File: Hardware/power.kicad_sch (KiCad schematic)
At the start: 18 parts, among them J3 JST_2mm_LiPo, U1 AP2112K-3.3, U2 MAX17048, U3 MCP73831

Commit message: Change to dedicated header format.
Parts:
- added D2: BAT60A, SparkFun-Semiconductor-Standard:SOD-323, symbol SparkFun-DiscreteSemi:D_Schottky_3A_10V_0.28V
- added J2: 1x10, SparkFun-Connector:1x10_Locking, symbol SparkFun-Connector:GNSS_Shield_10
- added J4: 1x09, SparkFun-Connector:1x09_Locking, symbol SparkFun-Connector:GNSS_Shield_9
- R13: value 10k -> 100k; symbol SparkFun-Resistor:10k_0603 -> SparkFun-Resistor:100k_0603; PROD_ID RES-00824 -> RES-07828
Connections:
- net 3V3_EN: now also J2.2 (Pin_2)
- net 5V: now also D2.C, J4.2 (Pin_8)
- net GND: now also J2.10 (Pin_10), J4.1 (Pin_9)
- net SCL: now also J2.7 (Pin_7)
- net SDA: now also J2.8 (Pin_8)
- net VBATT: now also D2.A
- new net Main-RX: J4.4 (Pin_6)
- new net Main-TX: J4.5 (Pin_5)
- new net SD_CD: J2.6 (Pin_6)
- new net SHLD_PICO: J4.7 (Pin_3)
- new net SHLD_POCI: J4.8 (Pin_2)
- new net SHLD_SCK: J4.9 (Pin_1)
- new net SHLD_~{CS}: J4.6 (Pin_4)
- no-connect marks 1 -> 6
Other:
- note added: "If 5V is present, LiPo charging commences. If 5V is absent, battery provides VBATT to mainboard. 3.3V is not provided to mainboard. 5V/VBATT powers local 3.3V_P."
- note added: "Shield Connectors"

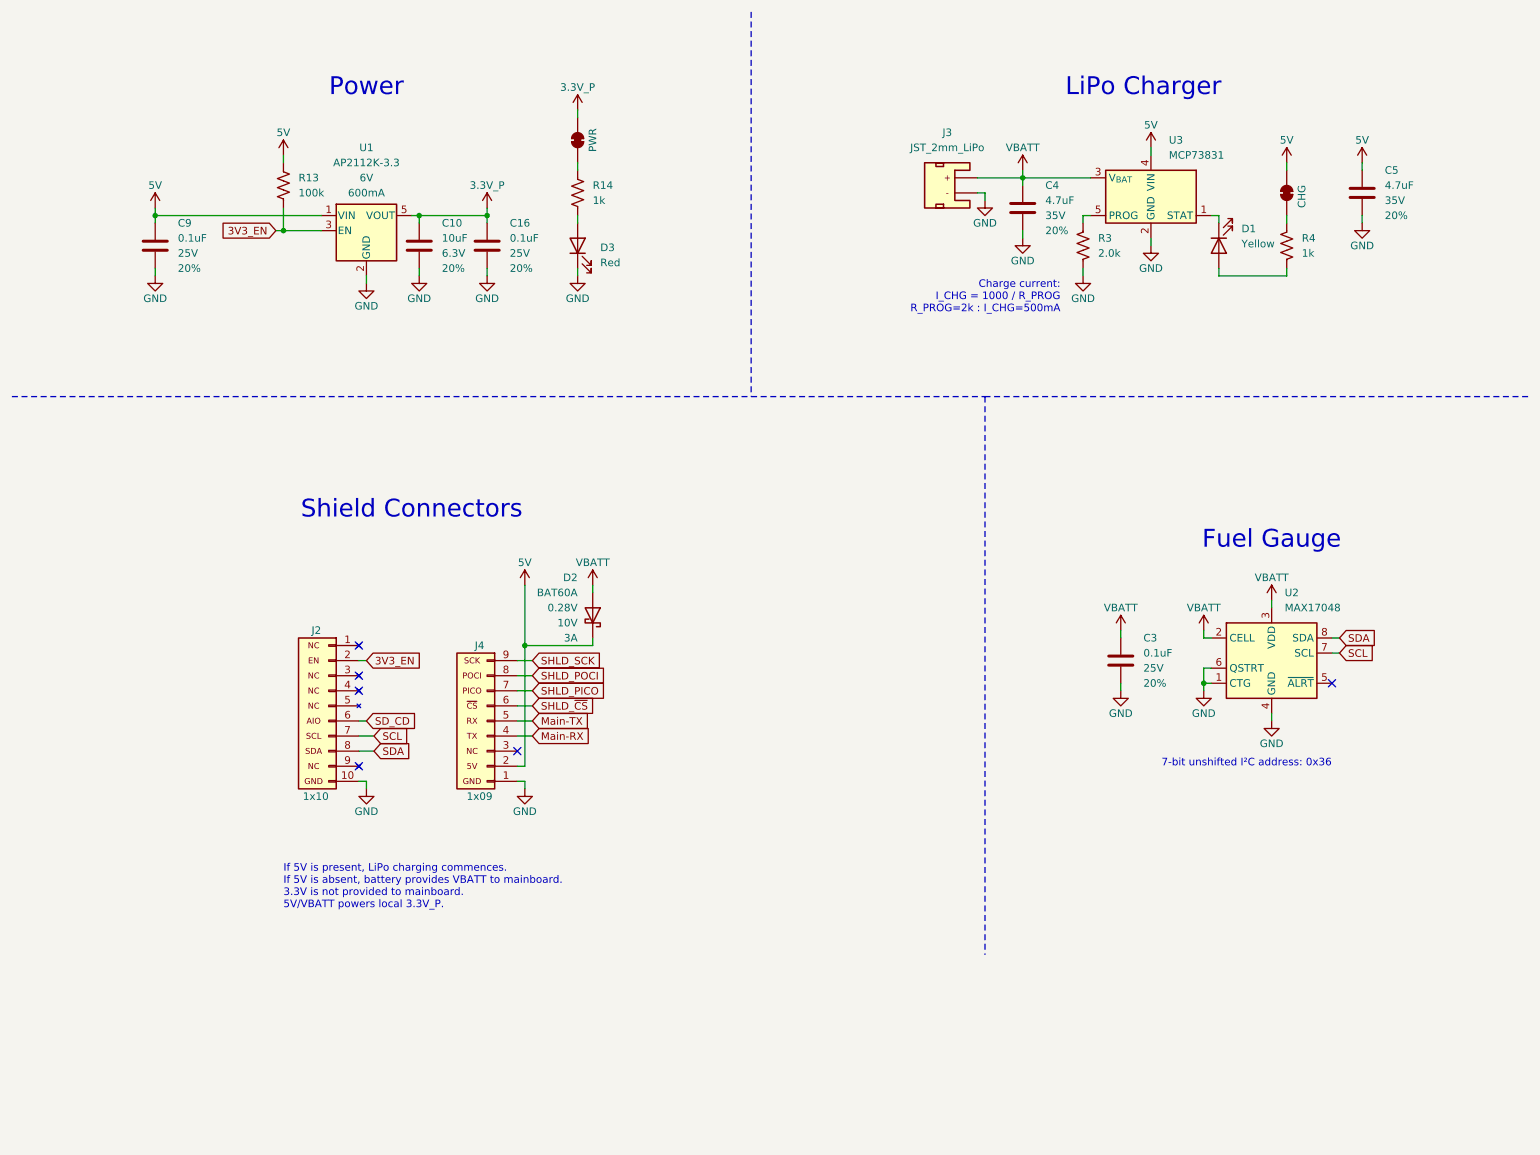
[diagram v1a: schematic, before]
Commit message: Add LM66200 battery switch
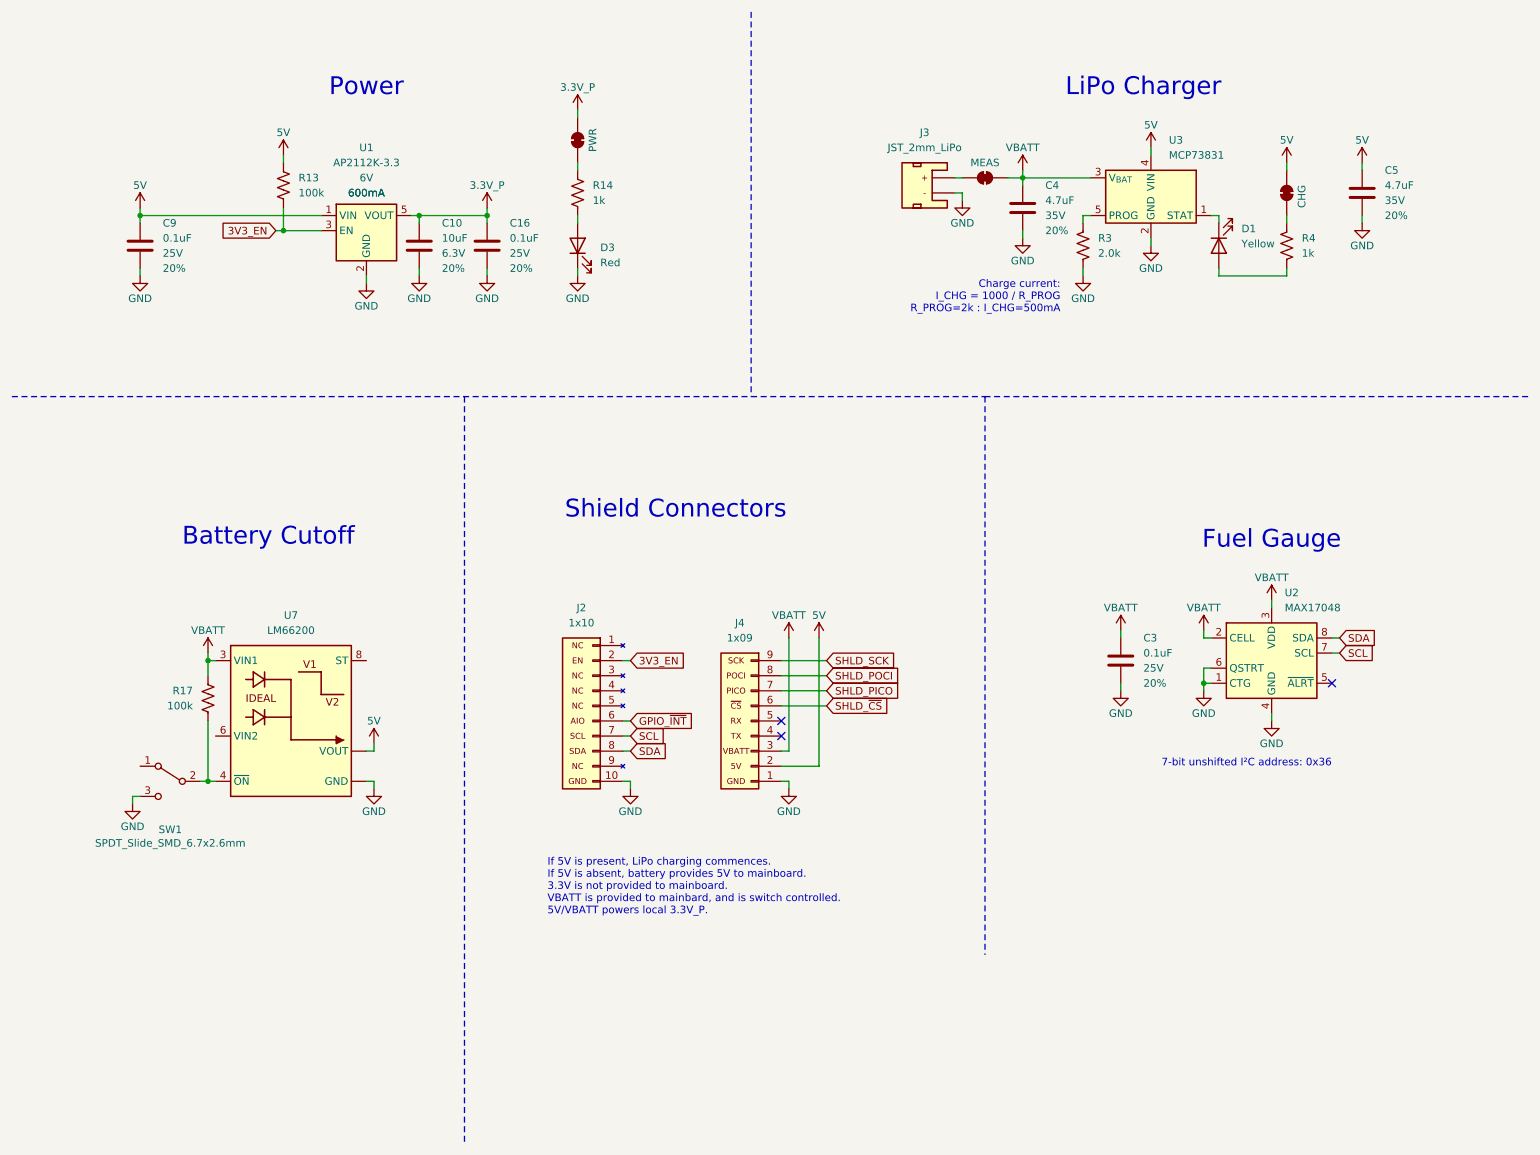
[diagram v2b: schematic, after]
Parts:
- removed D2: BAT60A, SparkFun-Semiconductor-Standard:SOD-323, symbol SparkFun-DiscreteSemi:D_Schottky_3A_10V_0.28V
- added JP5: MEAS, SparkFun-Jumper:Jumper_2_PTH_SMD_Combo-NC, symbol SparkFun-Jumper:Jumper_Measure
- added R17: 100k, SparkFun-Resistor:R_0603_1608Metric, symbol SparkFun-Resistor:100k_0603
- added SW1: SPDT_Slide_SMD_6.7x2.6mm, SparkFun-Switch:Slide_SPST_SMD_6.7x2.6mm, symbol SparkFun-Switch:SPDT_Slide_SMD_6.7x2.6mm
- added U7: LM66200, SparkFun-Semiconductor-Standard:SOT-583-8, symbol SparkFun-IC-Power:LM66200
- J2: symbol SparkFun-Connector:GNSS_Shield_10 -> SparkFun-Connector:Portability_Shield_10
- J4: symbol SparkFun-Connector:GNSS_Shield_9 -> SparkFun-Connector:Portability_Shield_9
- U1: IMax (none) -> 600mA
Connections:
- net 5V: now also U7.2 (VOUT), U7.7 (VOUT)
- net GND: now also SW1.3 (C), U7.1 (GND), U7.5 (GND)
- net VBATT: now also J4.3, JP5.2 (B), R17.1, U7.3 (VIN1); no longer J3.2 (+)
- net Main-RX: no longer names the net of J4.4
- net Main-TX: no longer names the net of J4.5
- net SD_CD renamed GPIO_~{INT}
- new net: R17.2, SW1.2, U7.4 (~{ON})
- new net: J3.2 (+), JP5.1 (A)
- no-connect marks 6 -> 3
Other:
- note added: "Battery Cutoff"
- note added: "If 5V is present, LiPo charging commences. If 5V is absent, battery provides 5V to mainboard. 3.3V is not provided to mainboard. VBATT is provided to mainbard, and is switch controlled. 5V/VBATT powers local 3.3V_P."
- note removed: "If 5V is present, LiPo charging commences. If 5V is absent, battery provides VBATT to mainboard. 3.3V is not provided to mainboard. 5V/VBATT powers local 3.3V_P."
- title: (none) -> SparkFun Portable Shield
- moved on the sheet: C9, J2, J3, J4
